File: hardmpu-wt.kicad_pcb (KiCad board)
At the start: 2 copper layers, 106 x 95.3 mm, 50 parts, among them J1 MIDI, J2 User, J3 LineOut, J4 ISP, J5 JTAG, J6 Wavetable, J7 AuxOut, J8 XT Bus, U1 74HCT138, U10 78L05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

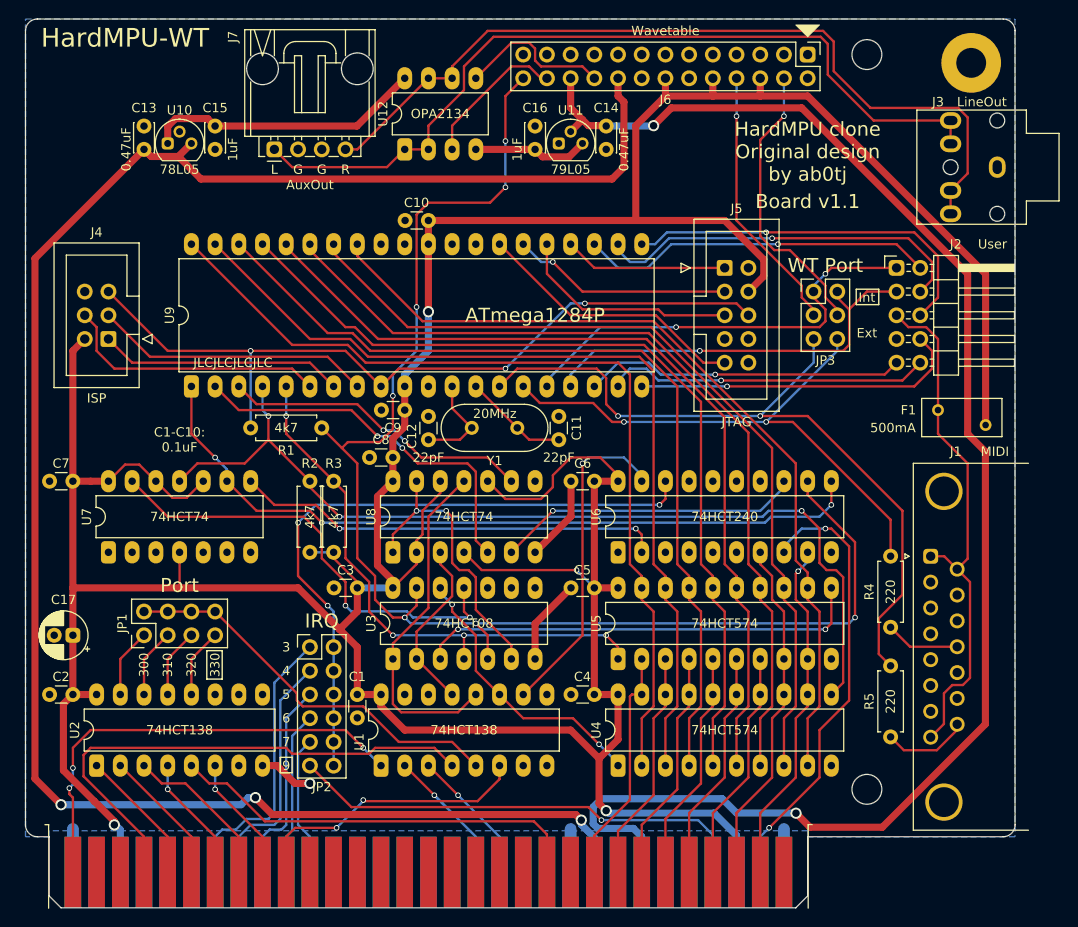
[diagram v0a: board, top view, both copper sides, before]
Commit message: Update to Kicad 6, fix DRC errors
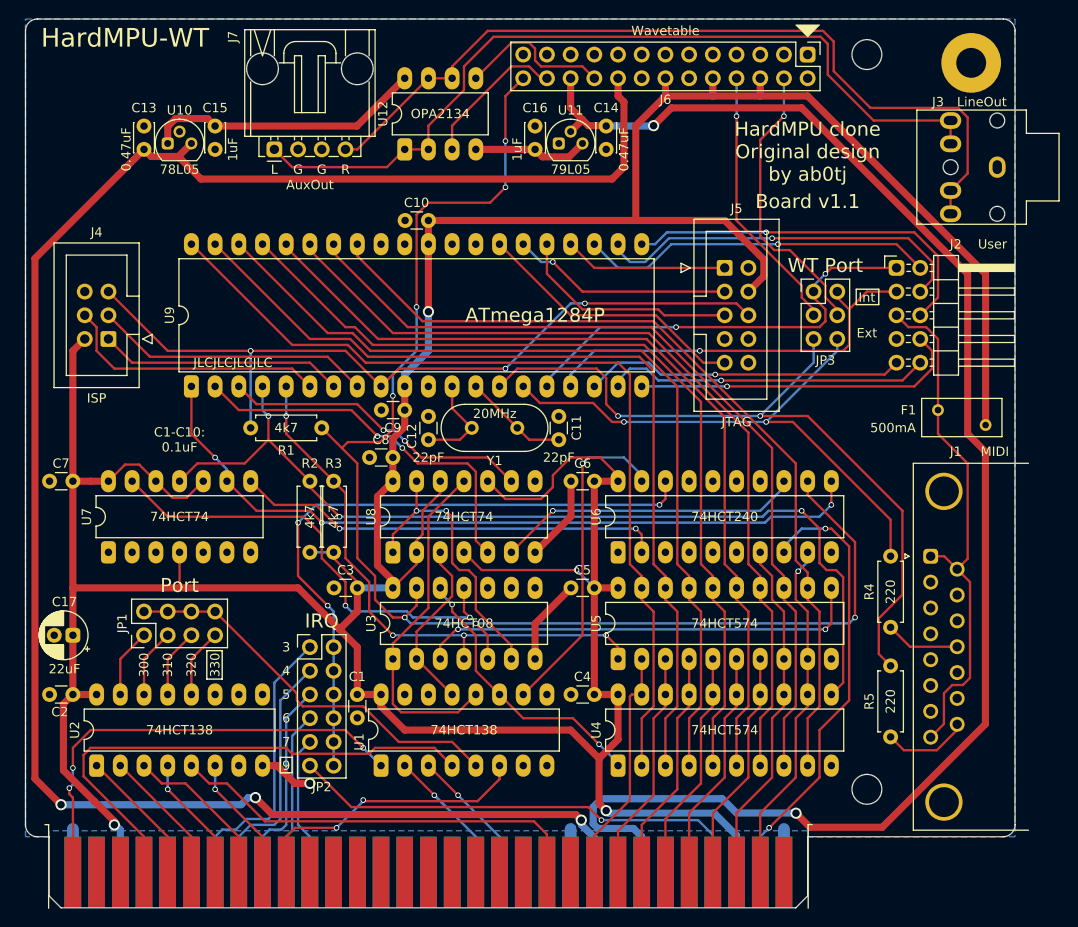
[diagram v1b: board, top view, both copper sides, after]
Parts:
- C1, C10, C11, C12, C2, C3, C4, C5, C6, C7, C8, C9: footprint Capacitor_THT:C_Disc_D3.0mm_W1.6mm_P2.50mm -> hardmpu-wt:C_Disc_D3.0mm_W1.6mm_P2.50mm_small_ctyd
- C13, C14, C15, C16: footprint Capacitor_THT:C_Disc_D3.0mm_W2.0mm_P2.50mm -> hardmpu-wt:C_Disc_D3.0mm_W2.0mm_P2.50mm_small_ctyd
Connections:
- net /~AVRRST renamed /~{AVRRST}
- net /~CR renamed /~{CR}
- net /~CW renamed /~{CW}
- net /~DR renamed /~{DR}
- net /~DRCLK renamed /~{DRCLK}
- net /~DRR renamed /~{DRR}
- net /~DRRS renamed /~{DRRS}
- net /~DSR renamed /~{DSR}
- net /~DW renamed /~{DW}
- net /~IDR renamed /~{IDR}
- net /~IDRRS renamed /~{IDRRS}
- net /~IDW renamed /~{IDW}
- net /~IOCS renamed /~{IOCS}
- net /~IOR renamed /~{IOR}
- net /~IOW renamed /~{IOW}
- net ~RESET renamed ~{RESET}
- H3 pad 1: Net-(H3-Pad1) -> unconnected-(H3-Pad1)
- J1 pad 10: Net-(J1-Pad10) -> unconnected-(J1-Pad10)
- J1 pad 11: Net-(J1-Pad11) -> unconnected-(J1-Pad11)
- J1 pad 13: Net-(J1-Pad13) -> unconnected-(J1-Pad13)
- J1 pad 14: Net-(J1-Pad14) -> unconnected-(J1-Pad14)
- J1 pad 2: Net-(J1-Pad2) -> unconnected-(J1-Pad2)
- J1 pad 3: Net-(J1-Pad3) -> unconnected-(J1-Pad3)
- J1 pad 6: Net-(J1-Pad6) -> unconnected-(J1-Pad6)
- J1 pad 7: Net-(J1-Pad7) -> unconnected-(J1-Pad7)
- J5 pad 7: Net-(J5-Pad7) -> unconnected-(J5-Pad7)
- J5 pad 8: Net-(J5-Pad8) -> unconnected-(J5-Pad8)
- J6 pad 13: Net-(J6-Pad13) -> unconnected-(J6-Pad13)
- J6 pad 2: Net-(J6-Pad2) -> unconnected-(J6-Pad2)
- J8 pad 11: Net-(J8-Pad11) -> unconnected-(J8-Pad11)
- J8 pad 12: Net-(J8-Pad12) -> unconnected-(J8-Pad12)
- J8 pad 15: Net-(J8-Pad15) -> unconnected-(J8-Pad15)
- J8 pad 16: Net-(J8-Pad16) -> unconnected-(J8-Pad16)
- J8 pad 17: Net-(J8-Pad17) -> unconnected-(J8-Pad17)
- J8 pad 18: Net-(J8-Pad18) -> unconnected-(J8-Pad18)
- J8 pad 19: Net-(J8-Pad19) -> unconnected-(J8-Pad19)
- J8 pad 20: Net-(J8-Pad20) -> unconnected-(J8-Pad20)
- J8 pad 26: Net-(J8-Pad26) -> unconnected-(J8-Pad26)
- J8 pad 27: Net-(J8-Pad27) -> unconnected-(J8-Pad27)
- J8 pad 28: Net-(J8-Pad28) -> unconnected-(J8-Pad28)
- J8 pad 30: Net-(J8-Pad30) -> unconnected-(J8-Pad30)
- J8 pad 32: Net-(J8-Pad32) -> unconnected-(J8-Pad32)
- J8 pad 41: Net-(J8-Pad41) -> unconnected-(J8-Pad41)
- J8 pad 43: Net-(J8-Pad43) -> unconnected-(J8-Pad43)
- J8 pad 44: Net-(J8-Pad44) -> unconnected-(J8-Pad44)
- J8 pad 45: Net-(J8-Pad45) -> unconnected-(J8-Pad45)
- J8 pad 46: Net-(J8-Pad46) -> unconnected-(J8-Pad46)
- J8 pad 47: Net-(J8-Pad47) -> unconnected-(J8-Pad47)
- J8 pad 48: Net-(J8-Pad48) -> unconnected-(J8-Pad48)
- J8 pad 49: Net-(J8-Pad49) -> unconnected-(J8-Pad49)
- J8 pad 5: Net-(J8-Pad5) -> unconnected-(J8-Pad5)
- J8 pad 50: Net-(J8-Pad50) -> unconnected-(J8-Pad50)
- J8 pad 51: Net-(J8-Pad51) -> unconnected-(J8-Pad51)
- J8 pad 52: Net-(J8-Pad52) -> unconnected-(J8-Pad52)
- J8 pad 6: Net-(J8-Pad6) -> unconnected-(J8-Pad6)
- J8 pad 60: Net-(J8-Pad60) -> unconnected-(J8-Pad60)
- J8 pad 61: Net-(J8-Pad61) -> unconnected-(J8-Pad61)
- J8 pad 8: Net-(J8-Pad8) -> unconnected-(J8-Pad8)
- U1 pad 14: Net-(U1-Pad14) -> unconnected-(U1-Pad14)
- U1 pad 15: Net-(U1-Pad15) -> unconnected-(U1-Pad15)
- U1 pad 7: Net-(U1-Pad7) -> unconnected-(U1-Pad7)
- U1 pad 9: Net-(U1-Pad9) -> unconnected-(U1-Pad9)
- U2 pad 10: Net-(U2-Pad10) -> unconnected-(U2-Pad10)
- U2 pad 11: Net-(U2-Pad11) -> unconnected-(U2-Pad11)
- U2 pad 7: Net-(U2-Pad7) -> unconnected-(U2-Pad7)
- U2 pad 9: Net-(U2-Pad9) -> unconnected-(U2-Pad9)
- U3 pad 8: Net-(U3-Pad8) -> unconnected-(U3-Pad8)
- U6 pad 14: Net-(U6-Pad14) -> unconnected-(U6-Pad14)
- U6 pad 16: Net-(U6-Pad16) -> unconnected-(U6-Pad16)
- U6 pad 3: Net-(U6-Pad3) -> unconnected-(U6-Pad3)
- U6 pad 5: Net-(U6-Pad5) -> unconnected-(U6-Pad5)
- U7 pad 5: Net-(U7-Pad5) -> unconnected-(U7-Pad5)
- U7 pad 6: Net-(U7-Pad6) -> unconnected-(U7-Pad6)
- U8 pad 8: Net-(U8-Pad8) -> unconnected-(U8-Pad8)
- U9 pad 28: Net-(U9-Pad28) -> unconnected-(U9-Pad28)
- U9 pad 29: Net-(U9-Pad29) -> unconnected-(U9-Pad29)
- U9 pad 32: Net-(U9-Pad32) -> unconnected-(U9-Pad32)
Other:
- board size 106 x 95.3 mm -> 106 x 95.2 mm
- net class Default removed
- net class Power removed
